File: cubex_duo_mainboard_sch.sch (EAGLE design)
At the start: 5 parts, among them IC1 PIC32MX440F256H, IC2 A3979, IC3 A3979, IC4 A3979

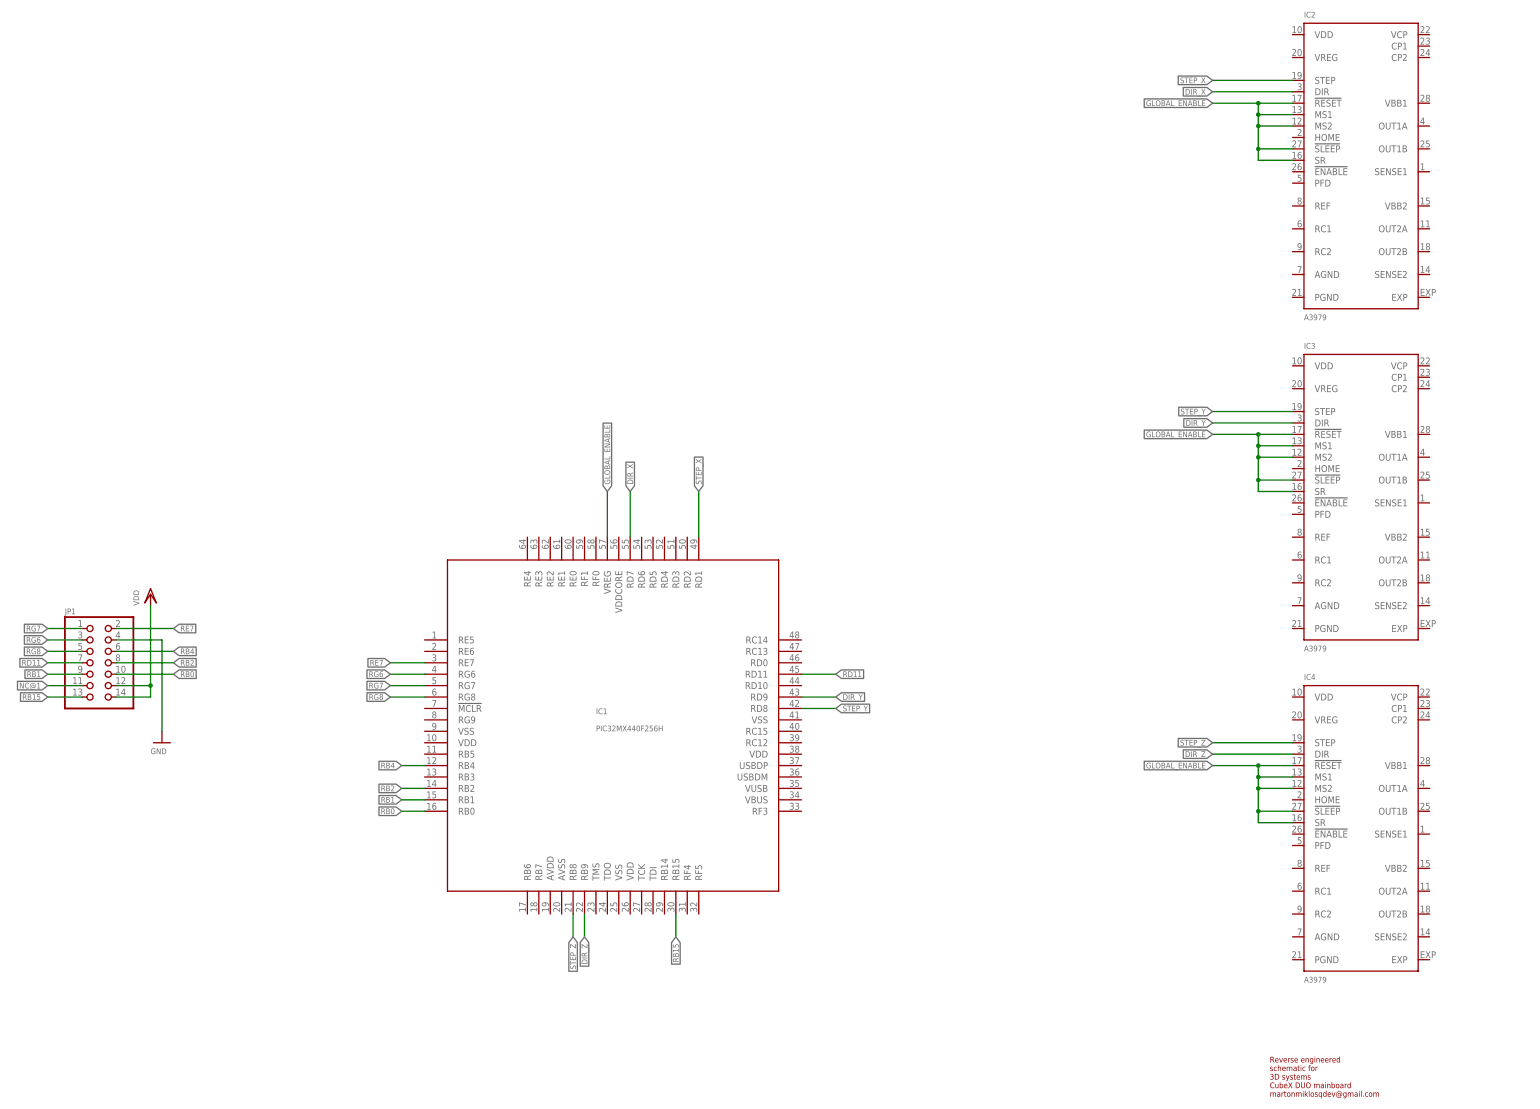
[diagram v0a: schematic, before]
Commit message: Added endswitch connection
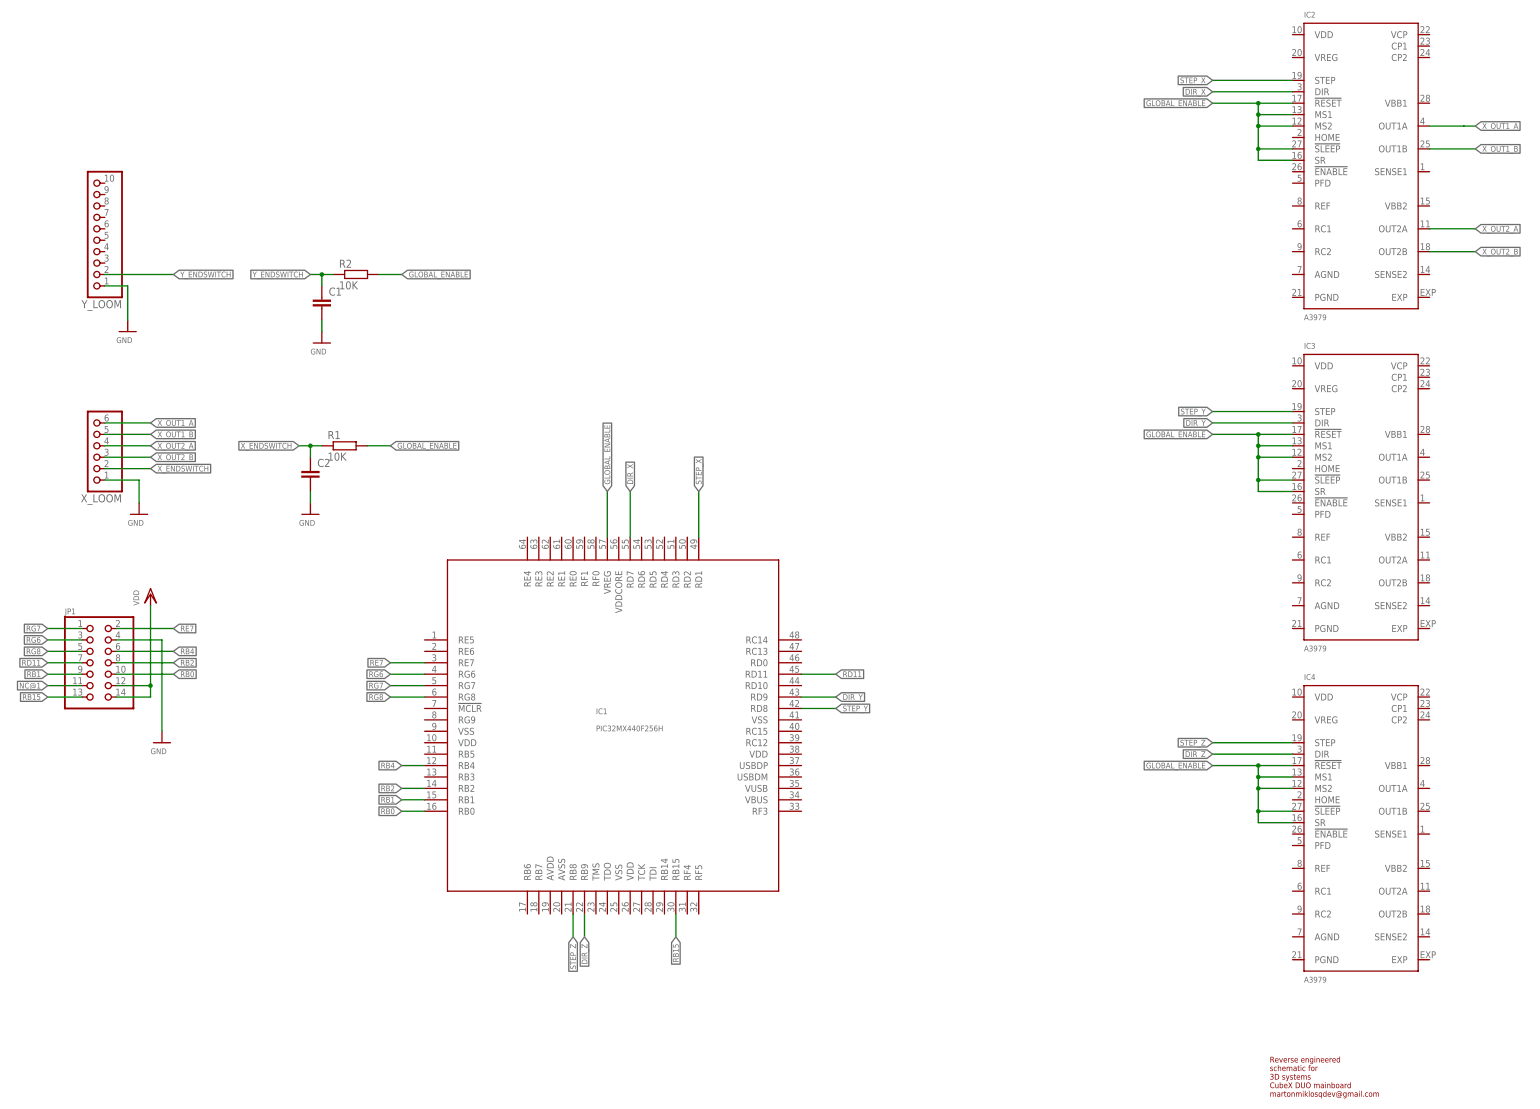
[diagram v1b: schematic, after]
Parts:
- added C1, C2: (no value), rcl:C-EUC0805
- added R1, R2: 10K, rcl:R-EU_R0805
- added X_LOOM: (no value), pinhead:PINHD-1X6
- added Y_LOOM: (no value), pinhead:PINHD-1X10
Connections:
- new net X_ENDSWITCH: C2.1, R1.1, X_LOOM.2
- new net X_OUT1_A: IC2.OUT1A, X_LOOM.6
- new net X_OUT1_B: IC2.OUT1B, X_LOOM.5
- new net X_OUT2_A: IC2.OUT2A, X_LOOM.4
- new net X_OUT2_B: IC2.OUT2B, X_LOOM.3
- new net Y_ENDSWITCH: C1.1, R2.1, Y_LOOM.2
- net GLOBAL_ENABLE: now also R1.2, R2.2
- net GND: now also C1.2, C2.2, X_LOOM.1, Y_LOOM.1
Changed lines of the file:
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@@
 <?xml version="1.0" encoding="utf-8"?>
 <!DOCTYPE eagle SYSTEM "eagle.dtd">
-<eagle version="9.2.1">
+<eagle version="9.6.2">
 <drawing>
 <settings>
@@
 <part name="JP1" library="pinhead" library_urn="urn:adsk.eagle:library:325" deviceset="PINHD-2X7" device="" package3d_urn="urn:adsk.eagle:package:22478/2"/>
 <part name="FRAME1" library="frames" deviceset="A3L-LOC" device=""/>
+<part name="Y_LOOM" library="pinhead" deviceset="PINHD-1X10" device=""/>
+<part name="GND2" library="supply1" deviceset="GND" device=""/>
+<part name="X_LOOM" library="pinhead" deviceset="PINHD-1X6" device=""/>
+<part name="GND3" library="supply1" deviceset="GND" device=""/>
+<part name="R1" library="rcl" deviceset="R-EU_" device="R0805" value="10K"/>
+<part name="C2" library="rcl" deviceset="C-EU" device="C0805"/>
+<part name="GND4" library="supply1" deviceset="GND" device=""/>
+<part name="R2" library="rcl" deviceset="R-EU_" device="R0805" value="10K"/>
+<part name="C1" library="rcl" deviceset="C-EU" device="C0805"/>
+<part name="GND5" library="supply1" deviceset="GND" device=""/>
 </parts>
 <sheets>
@@
 <attribute name="LAST_DATE_TIME" x="344.17" y="10.16" size="1.27" layer="94" font="vector"/>
 <attribute name="SHEET" x="357.505" y="5.08" size="1.27" layer="94" font="vector"/>
+</instance>
+<instance part="Y_LOOM" gate="A" x="30.48" y="198.12" smashed="yes" rot="R180">
+<attribute name="NAME" x="36.83" y="184.785" size="1.778" layer="95" rot="R180"/>
+<attribute name="VALUE" x="36.83" y="215.9" size="1.778" layer="96" rot="R180"/>
+</instance>
+<instance part="GND2" gate="1" x="38.1" y="177.8" smashed="yes">
+<attribute name="VALUE" x="35.56" y="175.26" size="1.27" layer="96" font="vector"/>
+</instance>
+<instance part="X_LOOM" gate="A" x="30.48" y="152.4" smashed="yes" rot="R180">
+<attribute name="NAME" x="36.83" y="141.605" size="1.778" layer="95" rot="R180"/>
+<attribute name="VALUE" x="36.83" y="162.56" size="1.778" layer="96" rot="R180"/>
+</instance>
+<instance part="GND3" gate="1" x="40.64" y="137.16" smashed="yes">
+<attribute name="VALUE" x="38.1" y="134.62" size="1.27" layer="96" font="vector"/>
+</instance>
+<instance part="R1" gate="G$1" x="86.36" y="152.4" smashed="yes">
+<attribute name="NAME" x="82.55" y="153.8986" size="1.778" layer="95"/>
+<attribute name="VALUE" x="82.55" y="149.098" size="1.778" layer="96"/>
+</instance>
+<instance part="C2" gate="G$1" x="78.74" y="147.32" smashed="yes">
+<attribute name="NAME" x="80.264" y="147.701" size="1.778" layer="95"/>
+<attribute name="VALUE" x="80.264" y="142.621" size="1.778" layer="96"/>
+</instance>
+<instance part="GND4" gate="1" x="78.74" y="137.16" smashed="yes">
+<attribute name="VALUE" x="76.2" y="134.62" size="1.27" layer="96" font="vector"/>
+</instance>
+<instance part="R2" gate="G$1" x="88.9" y="190.5" smashed="yes">
+<attribute name="NAME" x="85.09" y="191.9986" size="1.778" layer="95"/>
+<attribute name="VALUE" x="85.09" y="187.198" size="1.778" layer="96"/>
+</instance>
+<instance part="C1" gate="G$1" x="81.28" y="185.42" smashed="yes">
+<attribute name="NAME" x="82.804" y="185.801" size="1.778" layer="95"/>
+<attribute name="VALUE" x="82.804" y="180.721" size="1.778" layer="96"/>
+</instance>
+<instance part="GND5" gate="1" x="81.28" y="175.26" smashed="yes">
+<attribute name="VALUE" x="78.74" y="172.72" size="1.27" layer="96" font="vector"/>
 </instance>
 </instances>
@@
 <junction x="289.56" y="71.12"/>
 </segment>
+<segment>
+<pinref part="R1" gate="G$1" pin="2"/>
+<wire x1="91.44" y1="152.4" x2="96.52" y2="152.4" width="0.1524" layer="91"/>
+<label x="96.52" y="152.4" size="1.27" layer="95" font="vector" xref="yes"/>
+</segment>
+<segment>
+<pinref part="R2" gate="G$1" pin="2"/>
+<wire x1="93.98" y1="190.5" x2="99.06" y2="190.5" width="0.1524" layer="91"/>
+<label x="99.06" y="190.5" size="1.27" layer="95" font="vector" xref="yes"/>
+</segment>
 </net>
 <net name="STEP_X" class="0">
@@
 <wire x1="45.72" y1="109.22" x2="45.72" y2="88.9" width="0.1524" layer="91"/>
 <pinref part="JP1" gate="A" pin="4"/>
+</segment>
+<segment>
+<pinref part="Y_LOOM" gate="A" pin="1"/>
+<wire x1="33.02" y1="187.96" x2="38.1" y2="187.96" width="0.1524" layer="91"/>
+<pinref part="GND2" gate="1" pin="GND"/>
+<wire x1="38.1" y1="187.96" x2="38.1" y2="180.34" width="0.1524" layer="91"/>
+</segment>
+<segment>
+<pinref part="X_LOOM" gate="A" pin="1"/>
+<wire x1="33.02" y1="144.78" x2="40.64" y2="144.78" width="0.1524" layer="91"/>
+<pinref part="GND3" gate="1" pin="GND"/>
+<wire x1="40.64" y1="144.78" x2="40.64" y2="139.7" width="0.1524" layer="91"/>
+</segment>
+<segment>
+<pinref part="GND4" gate="1" pin="GND"/>
+<pinref part="C2" gate="G$1" pin="2"/>
+<wire x1="78.74" y1="139.7" x2="78.74" y2="142.24" width="0.1524" layer="91"/>
+</segment>
+<segment>
+<pinref part="GND5" gate="1" pin="GND"/>
+<pinref part="C1" gate="G$1" pin="2"/>
+<wire x1="81.28" y1="177.8" x2="81.28" y2="180.34" width="0.1524" layer="91"/>
 </segment>
 </net>
@@
 </segment>
 </net>
+<net name="Y_ENDSWITCH" class="0">
+<segment>
+<pinref part="Y_LOOM" gate="A" pin="2"/>
+<wire x1="33.02" y1="190.5" x2="48.26" y2="190.5" width="0.1524" layer="91"/>
+<label x="48.26" y="190.5" size="1.27" layer="95" font="vector" xref="yes"/>
+</segment>
+<segment>
+<pinref part="R2" gate="G$1" pin="1"/>
+<wire x1="83.82" y1="190.5" x2="81.28" y2="190.5" width="0.1524" layer="91"/>
+<pinref part="C1" gate="G$1" pin="1"/>
+<wire x1="81.28" y1="190.5" x2="81.28" y2="187.96" width="0.1524" layer="91"/>
+<wire x1="81.28" y1="190.5" x2="78.74" y2="190.5" width="0.1524" layer="91"/>
+<junction x="81.28" y="190.5"/>
+<label x="78.74" y="190.5" size="1.27" layer="95" font="vector" rot="R180" xref="yes"/>
+</segment>
+</net>
+<net name="X_OUT1_A" class="0">
+<segment>
+<pinref part="IC2" gate="P" pin="OUT1A"/>
+<wire x1="327.66" y1="223.52" x2="335.28" y2="223.52" width="0.1524" layer="91"/>
+<wire x1="335.28" y1="223.52" x2="337.82" y2="223.52" width="0.1524" layer="91"/>
+<label x="337.82" y="223.52" size="1.27" layer="95" font="vector" xref="yes"/>
+</segment>
+<segment>
+<pinref part="X_LOOM" gate="A" pin="6"/>
+<wire x1="33.02" y1="157.48" x2="43.18" y2="157.48" width="0.1524" layer="91"/>
+<label x="43.18" y="157.48" size="1.27" layer="95" font="vector" xref="yes"/>
+</segment>
+</net>
+<net name="X_OUT1_B" class="0">
+<segment>
+<pinref part="IC2" gate="P" pin="OUT1B"/>
+<wire x1="327.66" y1="218.44" x2="337.82" y2="218.44" width="0.1524" layer="91"/>
+<label x="337.82" y="218.44" size="1.27" layer="95" font="vector" xref="yes"/>
+</segment>
+<segment>
+<pinref part="X_LOOM" gate="A" pin="5"/>
+<wire x1="33.02" y1="154.94" x2="43.18" y2="154.94" width="0.1524" layer="91"/>
+<label x="43.18" y="154.94" size="1.27" layer="95" font="vector" xref="yes"/>
+</segment>
+</net>
+<net name="X_OUT2_A" class="0">
+<segment>
+<pinref part="IC2" gate="P" pin="OUT2A"/>
+<wire x1="327.66" y1="200.66" x2="337.82" y2="200.66" width="0.1524" layer="91"/>
+<label x="337.82" y="200.66" size="1.27" layer="95" font="vector" xref="yes"/>
+</segment>
+<segment>
+<pinref part="X_LOOM" gate="A" pin="4"/>
+<wire x1="33.02" y1="152.4" x2="43.18" y2="152.4" width="0.1524" layer="91"/>
+<label x="43.18" y="152.4" size="1.27" layer="95" font="vector" xref="yes"/>
+</segment>
+</net>
+<net name="X_OUT2_B" class="0">
+<segment>
+<pinref part="IC2" gate="P" pin="OUT2B"/>
+<wire x1="327.66" y1="195.58" x2="337.82" y2="195.58" width="0.1524" layer="91"/>
+<label x="337.82" y="195.58" size="1.27" layer="95" font="vector" xref="yes"/>
+</segment>
+<segment>
+<pinref part="X_LOOM" gate="A" pin="3"/>
+<wire x1="33.02" y1="149.86" x2="43.18" y2="149.86" width="0.1524" layer="91"/>
+<label x="43.18" y="149.86" size="1.27" layer="95" font="vector" xref="yes"/>
+</segment>
+</net>
+<net name="X_ENDSWITCH" class="0">
+<segment>
+<pinref part="X_LOOM" gate="A" pin="2"/>
+<wire x1="33.02" y1="147.32" x2="43.18" y2="147.32" width="0.1524" layer="91"/>
+<label x="43.18" y="147.32" size="1.27" layer="95" font="vector" xref="yes"/>
+</segment>
+<segment>
+<pinref part="R1" gate="G$1" pin="1"/>
+<wire x1="81.28" y1="152.4" x2="78.74" y2="152.4" width="0.1524" layer="91"/>
+<pinref part="C2" gate="G$1" pin="1"/>
+<wire x1="78.74" y1="152.4" x2="78.74" y2="149.86" width="0.1524" layer="91"/>
+<wire x1="78.74" y1="152.4" x2="76.2" y2="152.4" width="0.1524" layer="91"/>
+<junction x="78.74" y="152.4"/>
+<label x="76.2" y="152.4" size="1.27" layer="95" font="vector" rot="R180" xref="yes"/>
+</segment>
+</net>
